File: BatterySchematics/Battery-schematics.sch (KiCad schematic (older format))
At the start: 22 parts, among them J1 Conn_01x02, J2 Conn_Coaxial_x2, J3 Conn_Coaxial, K1 DIPxx-1Axx-11x, K2 DIPxx-1Axx-11x, K3 DIPxx-1Axx-11x, Q1 2N7000, Q2 2N7000, Q3 2N7000, SW1 SW_SPST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

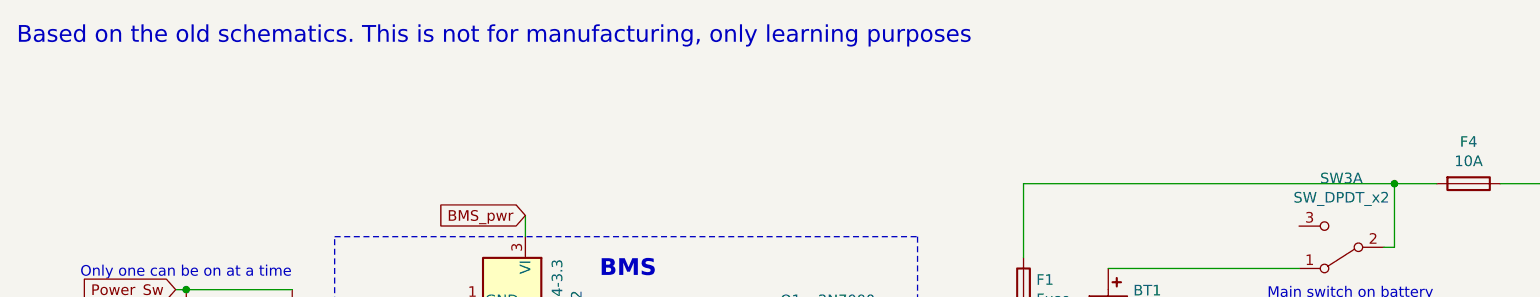
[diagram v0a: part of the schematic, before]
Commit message: Added folder for blockdiagrams via git
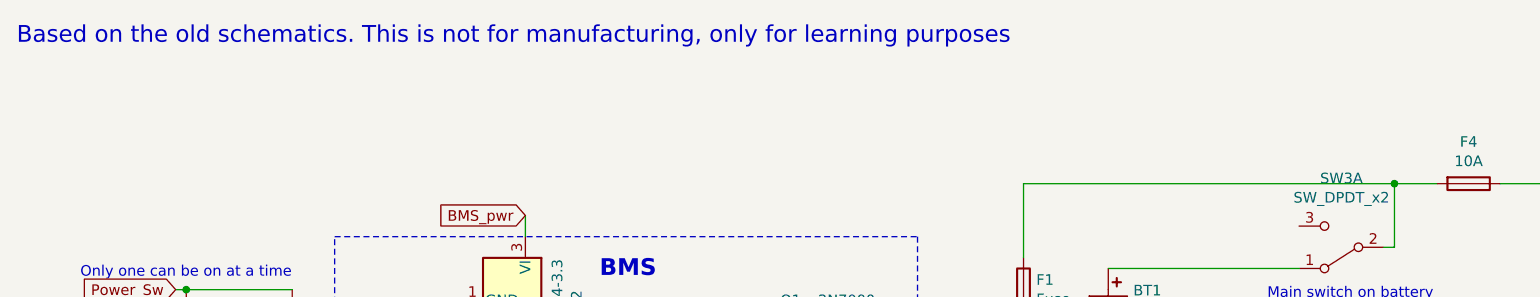
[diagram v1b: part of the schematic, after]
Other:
- note added: "Based on the old schematics. This is not for manufacturing, only for learning purposes"
- note removed: "Based on the old schematics. This is not for manufacturing, only learning purposes"
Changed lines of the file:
@@
 	4550 2050 4500 2050
 Text Notes 550  700  0    79   ~ 0
-Based on the old schematics. This is not for manufacturing, only learning purposes
+Based on the old schematics. This is not for manufacturing, only for learning purposes
 Text Notes 6450 1900 0    50   ~ 0
 Main switch on battery

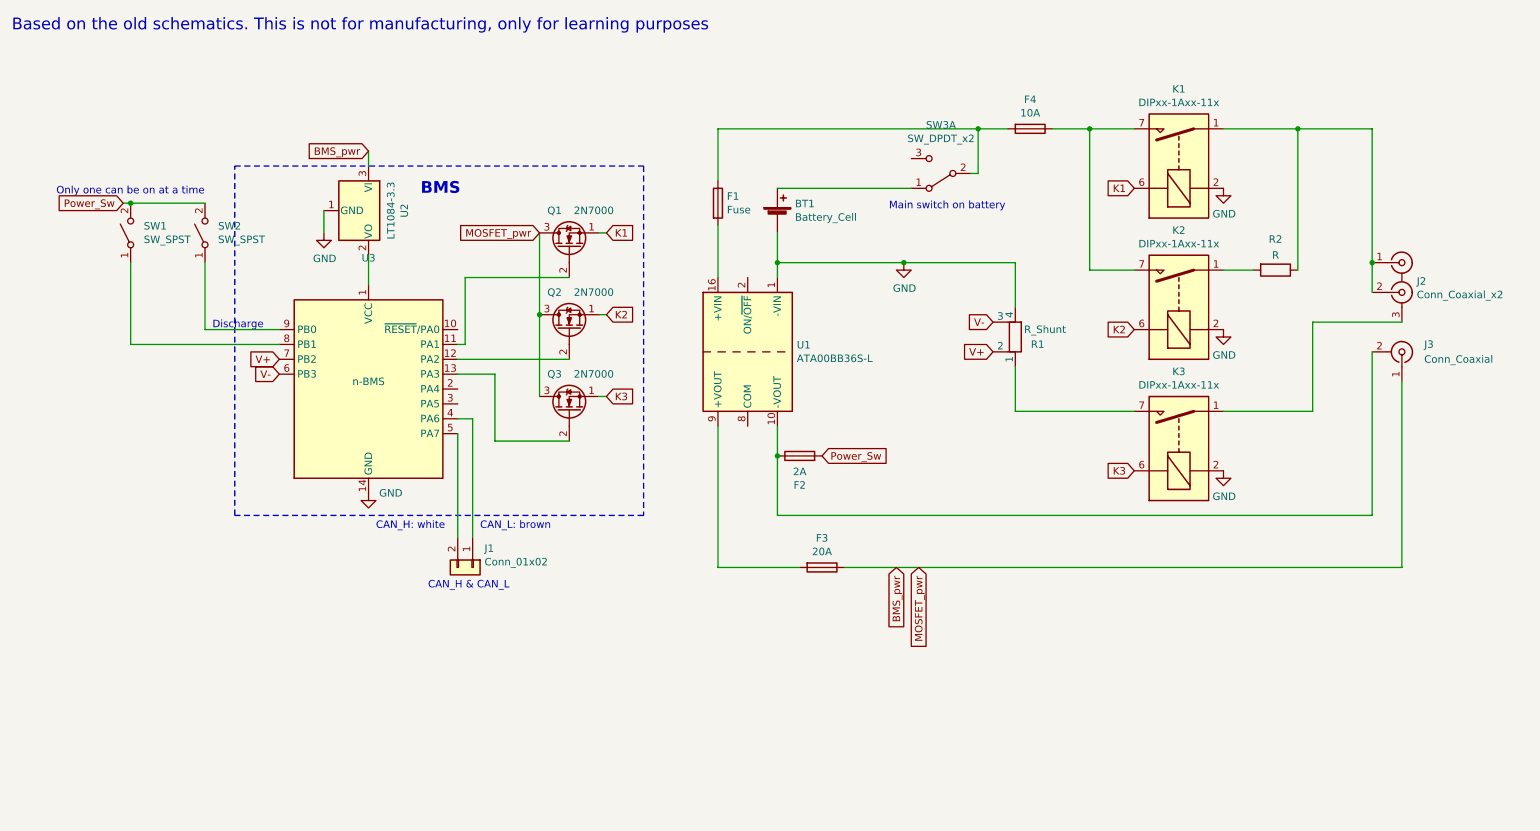
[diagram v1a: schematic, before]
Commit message: updated battery schematics
Signed-off-by: Mojitas <47667093+Mojitas@users.noreply.github.com>
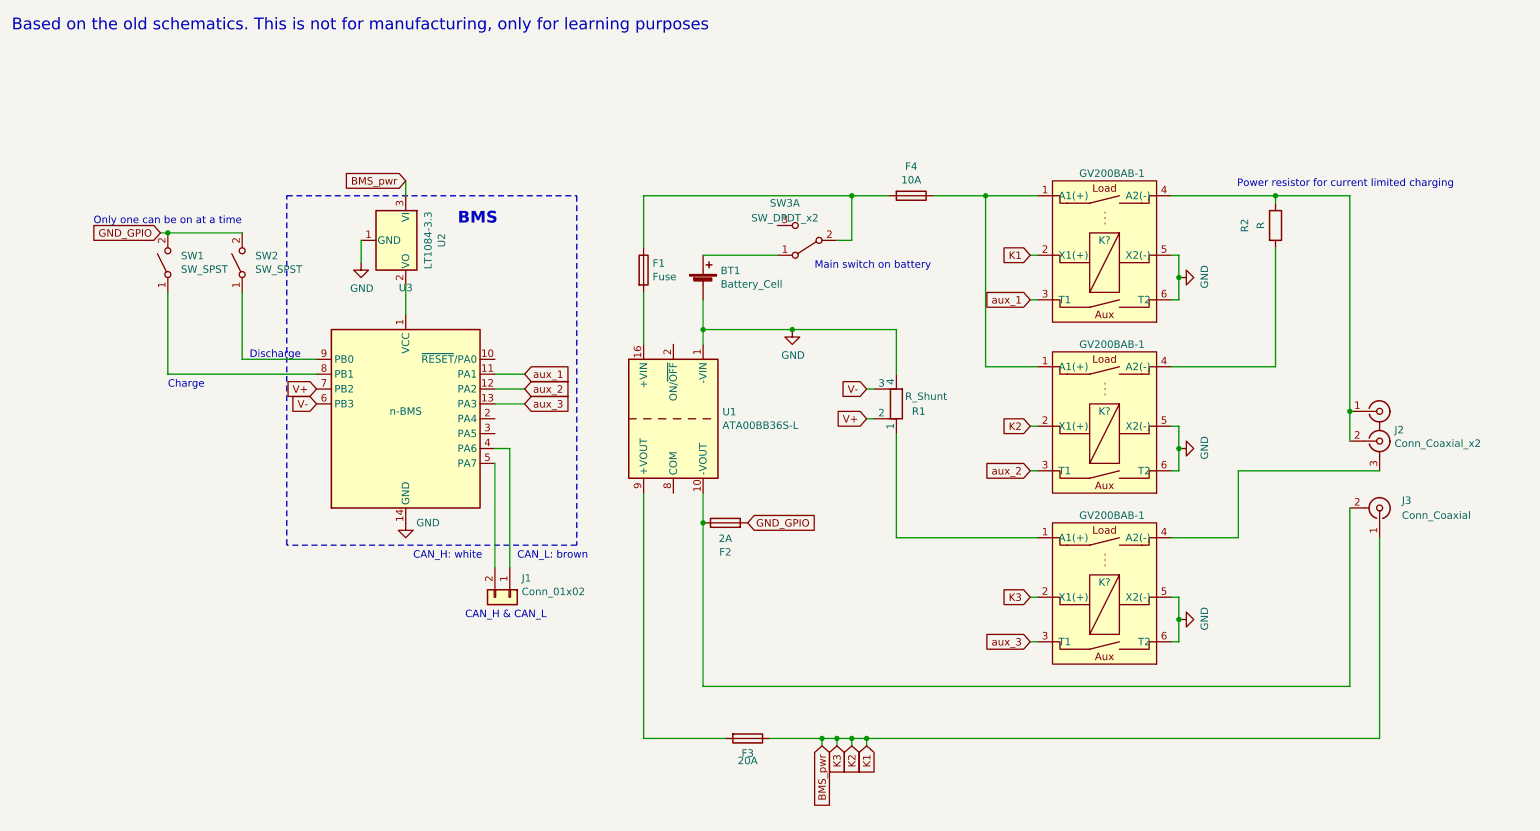
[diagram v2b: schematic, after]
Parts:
- removed K1, K2, K3: DIPxx-1Axx-11x, Relay_THT:Relay_StandexMeder_DIP_LowProfile, symbol Relay:DIPxx-1Axx-11x
- removed Q1, Q2, Q3: 2N7000, Package_TO_SOT_THT:TO-92_Inline, symbol Transistor_FET:2N7000
- added K? (x3): GV200BAB-1, symbol Battery-schematics-rescue:GV200BAB-1-Solar_team_library
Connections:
- net BMS_pwr: now also K?.2 (X1(+)), K?.2 (X1(+)), K?.2 (X1(+))
- net GND: now also K?.5 (X2(-)), K?.5 (X2(-)), K?.5 (X2(-)), K?.6 (T2), K?.6 (T2), K?.6 (T2)
- net at F4.1: now also K?.1 (A1(+)), K?.1 (A1(+))
- net at J2.1 (IN1), J2.2 (IN2), R2.1: now also K?.4 (A2(-))
- net at R2.2: now also K?.4 (A2(-))
- net at J2.3 (EXT): now also K?.4 (A2(-))
- net at R1.1: now also K?.1 (A1(+))
- net aux_3: now reaches U3.13 (PA3)
- net aux_3: now also K?.3 (T1)
- net aux_2: now reaches U3.12 (PA2)
- net aux_2: now also K?.3 (T1)
- net aux_1: now reaches U3.11 (PA1)
- net aux_1: now also K?.3 (T1)
- net Power_Sw renamed GND_GPIO
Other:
- note added: "Charge"
- note added: "Power resistor for current limited charging"
- moved on the sheet: BT1, F1, F2, F3, F4, J1, J2, J3, R1, R2, SW1, SW2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
